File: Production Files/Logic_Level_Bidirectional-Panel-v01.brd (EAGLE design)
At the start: 123.4 x 118.9 mm, 1011 parts, among them Q1 BSS138, Q10 BSS138, Q100 BSS138, Q101 BSS138, Q102 BSS138, Q103 BSS138, Q104 BSS138, Q105 BSS138, Q106 BSS138, Q107 BSS138, Q108 BSS138, Q109 BSS138, Q11 BSS138, Q110 BSS138, Q111 BSS138, Q112 BSS138, Q113 BSS138, Q114 BSS138, Q115 BSS138, Q116 BSS138, Q117 BSS138, Q118 BSS138, Q119 BSS138, Q12 BSS138, Q120 BSS138, Q121 BSS138, Q122 BSS138, Q123 BSS138, Q124 BSS138, Q125 BSS138, Q126 BSS138, Q127 BSS138, Q128 BSS138, Q129 BSS138, Q13 BSS138, Q130 BSS138, Q131 BSS138, Q132 BSS138, Q133 BSS138, Q134 BSS138, Q135 BSS138, Q136 BSS138, Q137 BSS138, Q138 BSS138, Q139 BSS138, Q14 BSS138, Q140 BSS138, Q141 BSS138, Q142 BSS138, Q143 BSS138, Q144 BSS138, Q145 BSS138, Q146 BSS138, Q147 BSS138, Q148 BSS138, Q149 BSS138, Q15 BSS138, Q150 BSS138, Q151 BSS138, Q152 BSS138, Q153 BSS138, Q154 BSS138, Q155 BSS138, Q156 BSS138, Q157 BSS138, Q158 BSS138, Q159 BSS138, Q16 BSS138, Q160 BSS138, Q161 BSS138, Q162 BSS138, Q163 BSS138, Q164 BSS138, Q165 BSS138, Q166 BSS138, Q167 BSS138, Q168 BSS138, Q169 BSS138, Q17 BSS138, Q170 BSS138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

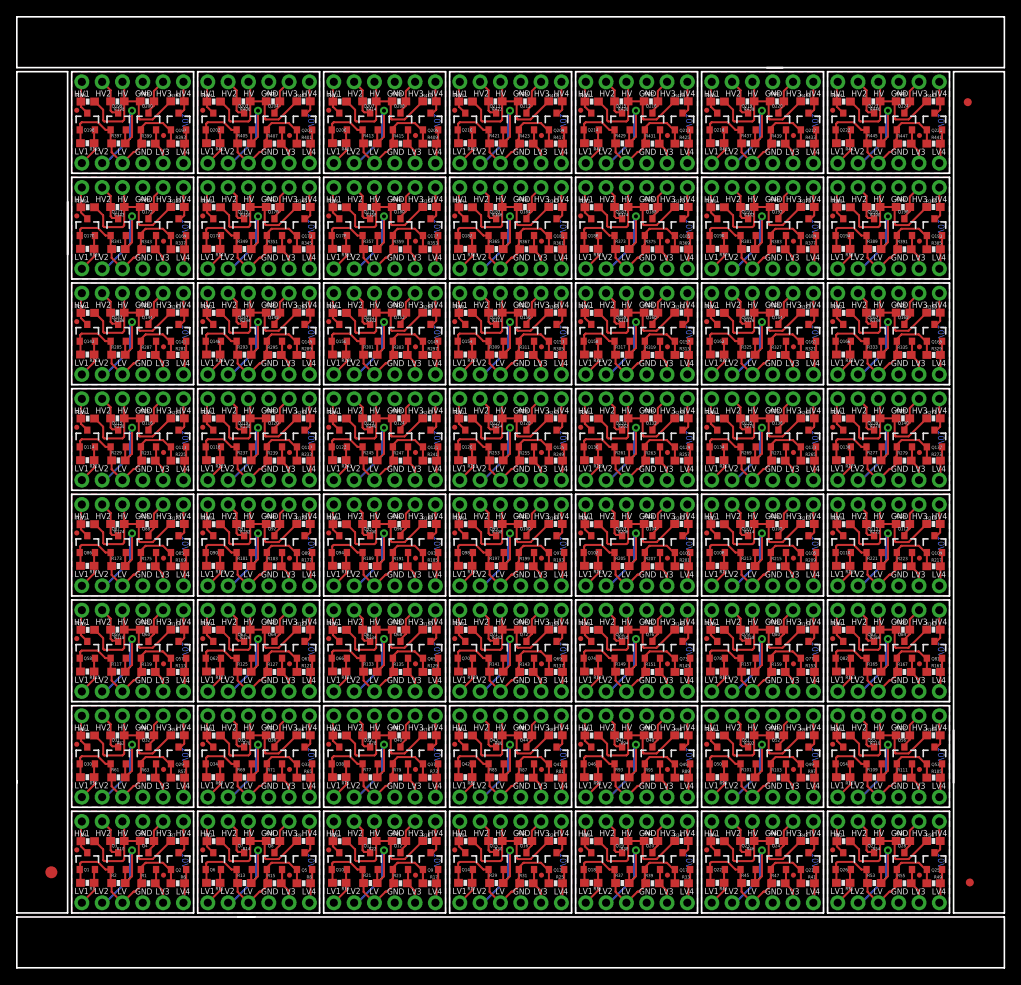
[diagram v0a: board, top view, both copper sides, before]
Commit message: Recreated Panels both normal and Giant
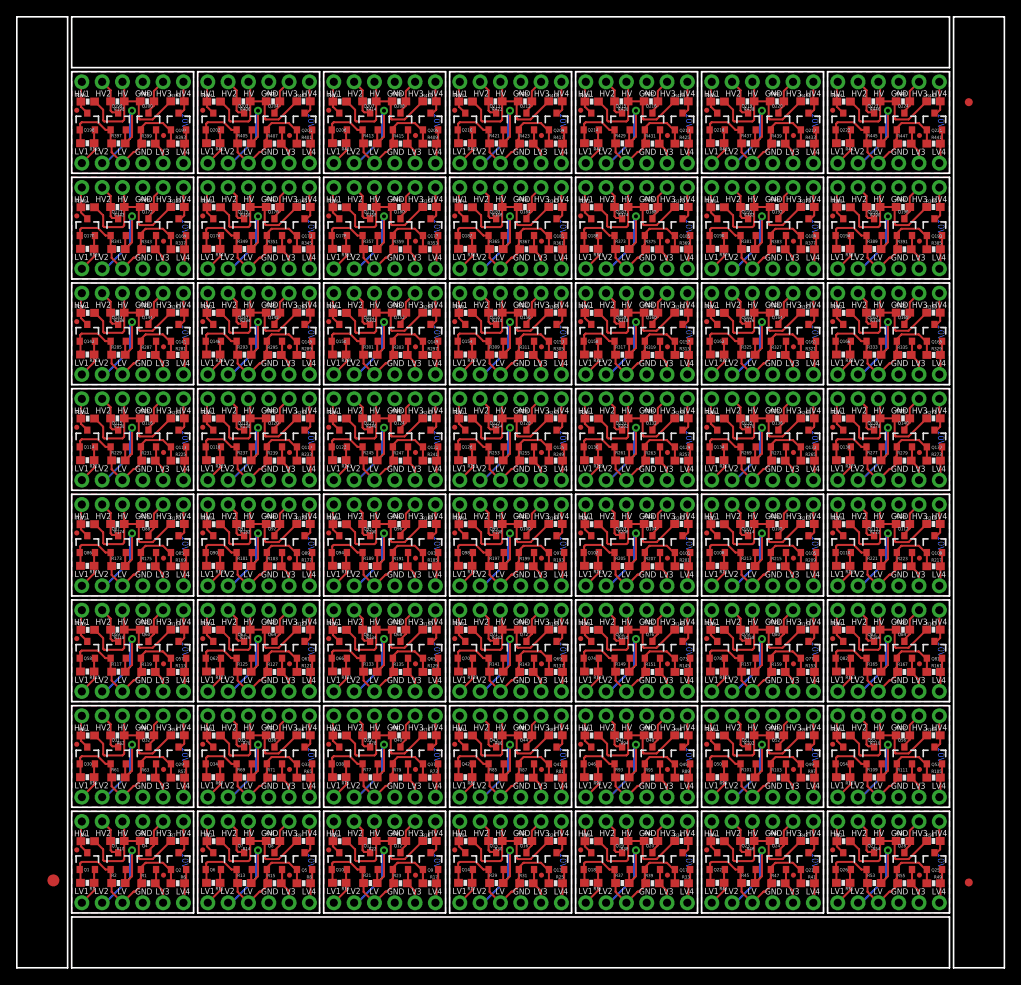
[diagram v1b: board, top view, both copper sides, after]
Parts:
- moved E$1 1.05 mm to (4.57, 10.9)
- moved E$4 0.13 mm to (119.0, 10.7)
- moved E$5 0.13 mm to (119.0, 108.2)
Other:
- outline, holes or cut-outs redrawn
